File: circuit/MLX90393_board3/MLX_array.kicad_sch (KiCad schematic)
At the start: 4 parts

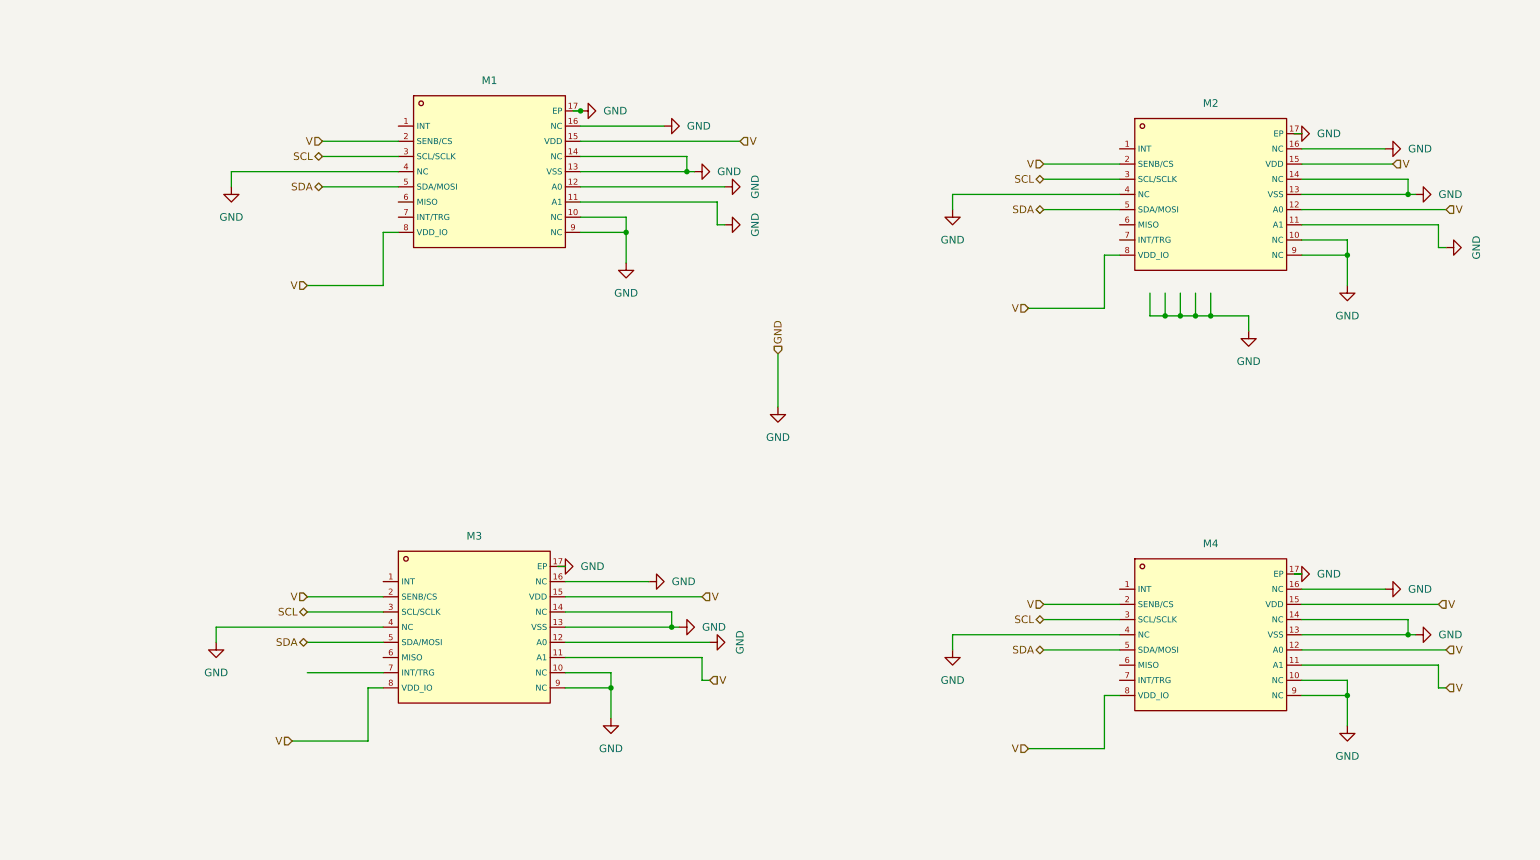
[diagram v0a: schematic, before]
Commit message: refactored socketio
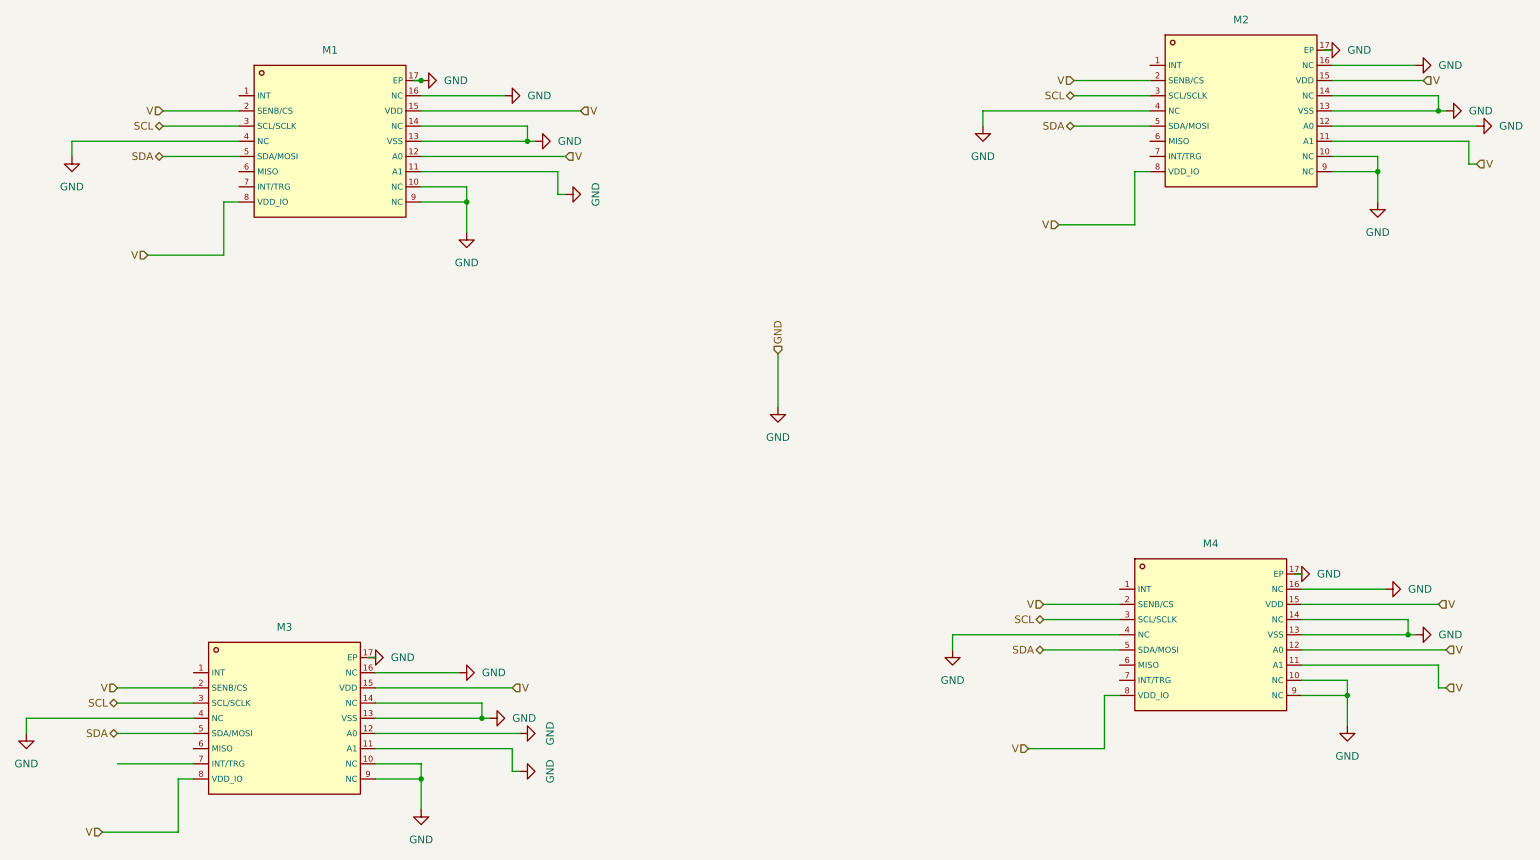
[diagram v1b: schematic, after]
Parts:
- M1: LCSC C2649492 -> C1526572
- M2: LCSC C1526573 -> C1526571
- M3: LCSC C2152977 -> C2649492
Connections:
- net GND: now also M2.12 (A0), M3.11 (A1); no longer M1.12 (A0), M2.11 (A1)
- net V: now also M1.12 (A0), M2.11 (A1); no longer M2.12 (A0), M3.11 (A1)
